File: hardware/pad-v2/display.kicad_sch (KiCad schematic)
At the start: 4 parts, among them J501 Display 1.69in ST7789V3, Q501 AO3401A

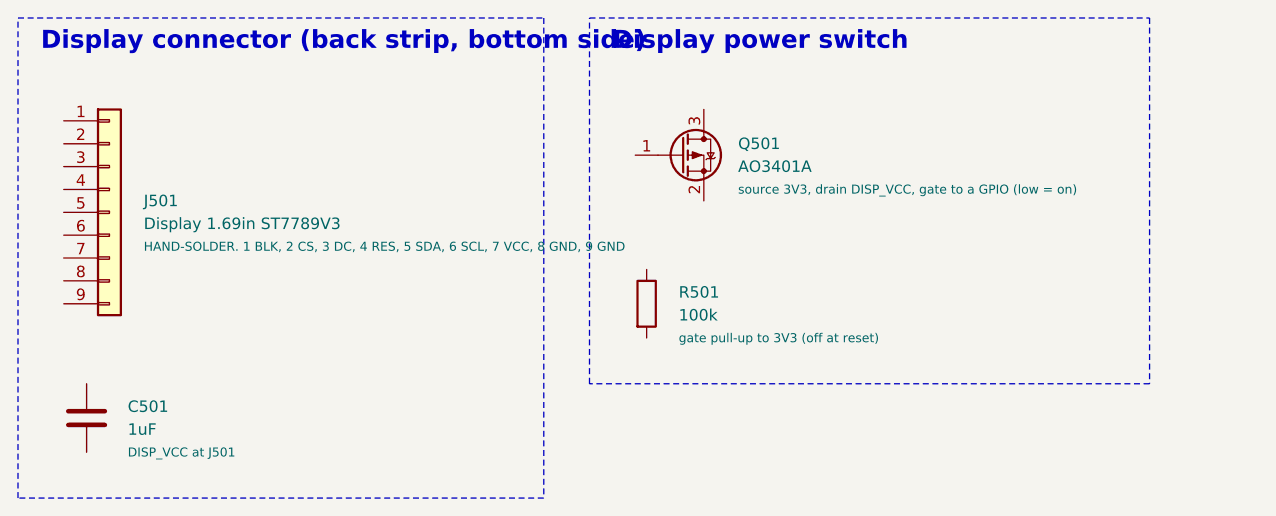
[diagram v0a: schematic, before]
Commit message: Pad v2: GPIO map for routing, PAD_WIRING.md (component-by-component), connection model + checker; battery 2-pin + NTC header, USB-C to the front edge, LED chain starts at key 9
Co-Authored-By: Claude Opus 5.5 <noreply@anthropic.com>
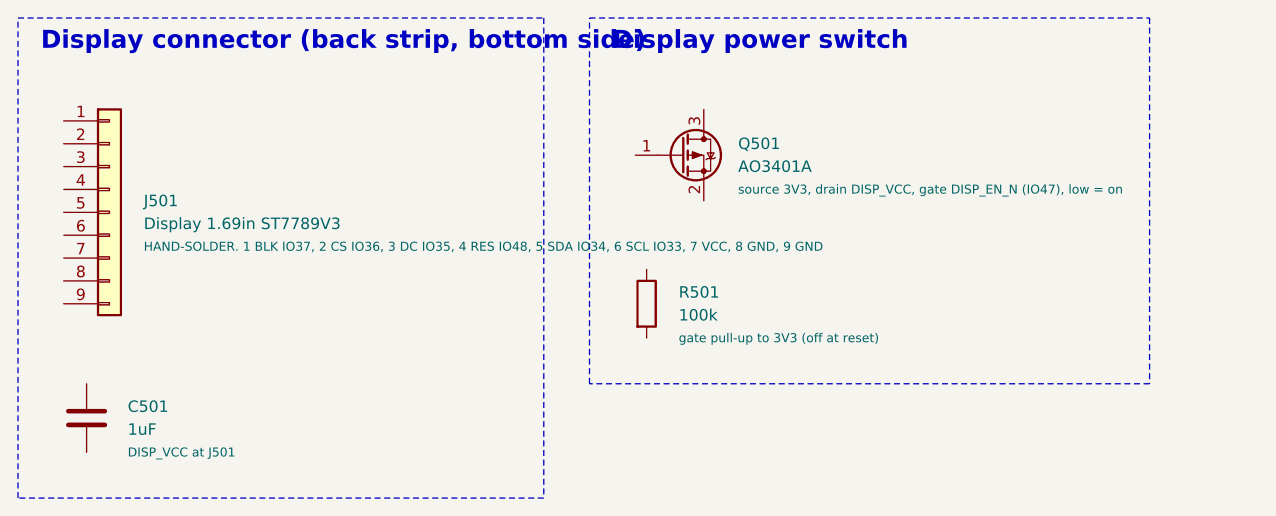
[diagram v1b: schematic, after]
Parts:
- J501: Note HAND-SOLDER. 1 BLK, 2 CS, 3 DC, 4 RES, 5 SDA, 6 SCL, 7 VCC,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 -> HAND-SOLDER. 1 BLK IO37, 2 CS IO36, 3 DC IO35, 4 RES IO48, 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
- Q501: Note source 3V3, drain DISP_VCC, gate to a GPIO (low = on) -> source 3V3, drain DISP_VCC, gate DISP_EN_N (IO47), low = on
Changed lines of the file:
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@@
 			)
 		)
-		(property "Note" "HAND-SOLDER. 1 BLK, 2 CS, 3 DC, 4 RES, 5 SDA, 6 SCL, 7 VCC, 8 GND, 9 GND"
+		(property "Note" "HAND-SOLDER. 1 BLK IO37, 2 CS IO36, 3 DC IO35, 4 RES IO48, 5 SDA IO34, 6 SCL IO33, 7 VCC, 8 GND, 9 GND"
 			(at 26.67 43.18 0)
 			(show_name no)
@@
 		(instances
 			(project "pad-v2"
-				(path "/c348787c-35a6-4c40-81d7-0eeb948bfe4d/41e8144f-af4e-429a-84eb-e53a8ac26d50"
+				(path "/aa63e03b-1ac8-4926-b623-c7b31956768e/0f52c6a6-8bfa-4bd4-83e5-5c5f20abff80"
 					(reference "J501")
 					(unit 1)
@@
 		(instances
 			(project "pad-v2"
-				(path "/c348787c-35a6-4c40-81d7-0eeb948bfe4d/41e8144f-af4e-429a-84eb-e53a8ac26d50"
+				(path "/aa63e03b-1ac8-4926-b623-c7b31956768e/0f52c6a6-8bfa-4bd4-83e5-5c5f20abff80"
 					(reference "C501")
 					(unit 1)
@@
 			)
 		)
-		(property "Note" "source 3V3, drain DISP_VCC, gate to a GPIO (low = on)"
+		(property "Note" "source 3V3, drain DISP_VCC, gate DISP_EN_N (IO47), low = on"
 			(at 92.71 36.83 0)
 			(show_name no)
@@
 		(instances
 			(project "pad-v2"
-				(path "/c348787c-35a6-4c40-81d7-0eeb948bfe4d/41e8144f-af4e-429a-84eb-e53a8ac26d50"
+				(path "/aa63e03b-1ac8-4926-b623-c7b31956768e/0f52c6a6-8bfa-4bd4-83e5-5c5f20abff80"
 					(reference "Q501")
 					(unit 1)
@@
 		(instances
 			(project "pad-v2"
-				(path "/c348787c-35a6-4c40-81d7-0eeb948bfe4d/41e8144f-af4e-429a-84eb-e53a8ac26d50"
+				(path "/aa63e03b-1ac8-4926-b623-c7b31956768e/0f52c6a6-8bfa-4bd4-83e5-5c5f20abff80"
 					(reference "R501")
 					(unit 1)
